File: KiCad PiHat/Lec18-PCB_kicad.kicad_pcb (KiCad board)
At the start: 2 copper layers, 65 x 56 mm, 6 parts, among them P1 Conn_02x20_Odd_Even

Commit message: Ongoing work
Continued work on schematic and PCB
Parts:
- added J4: Motor_Driver_Left, Connector_PinSocket_2.54mm:PinSocket_1x04_P2.54mm_Vertical, F.Cu at (103.5, 45.9)
- added R1: 1k, Resistor_THT:R_Axial_DIN0207_L6.3mm_D2.5mm_P7.62mm_Horizontal, F.Cu at (132.7, 76.3)
- added R2: 1k, Resistor_THT:R_Axial_DIN0207_L6.3mm_D2.5mm_P7.62mm_Horizontal, F.Cu at (125.1, 81.4)
- added R3: 1k, Resistor_THT:R_Axial_DIN0207_L6.3mm_D2.5mm_P7.62mm_Horizontal, F.Cu at (121.1, 75.1)
- A1: value Arduino_Nano_v2.x -> Arduino_Nano
- moved A1 34.1 mm to (132.7, 71.3), turned to -90 degrees
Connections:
- net +3V3 renamed Net-(P1-Pad1)
- A1 pad 1: /GPIO15(RXD0) -> /GPIO14(TXD0_5V)
- A1 pad 29: unconnected-(A1-Pad29) -> GND
- A1 pad 30: unconnected-(A1-Pad30) -> +5V
- A1 pad 4: unconnected-(A1-Pad4) -> GND
- P1 pad 10: /GPIO15(RXD0) -> /GPIO15(RXD0_3.3V)
- P1 pad 2: +5V -> Net-(P1-Pad2)
- P1 pad 4: +5V -> Net-(P1-Pad2)

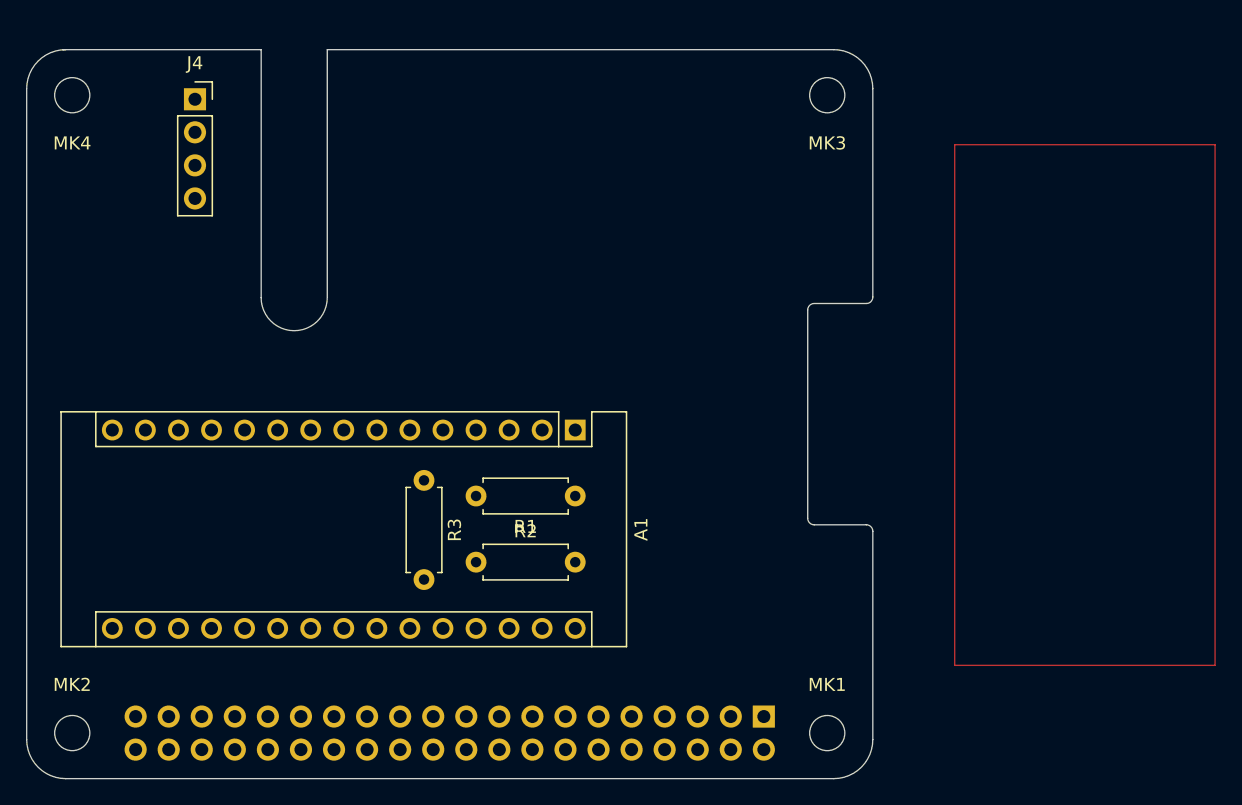
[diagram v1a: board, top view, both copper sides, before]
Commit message: Finished Schematic
Schematic finished. Sanity check and routing coming next
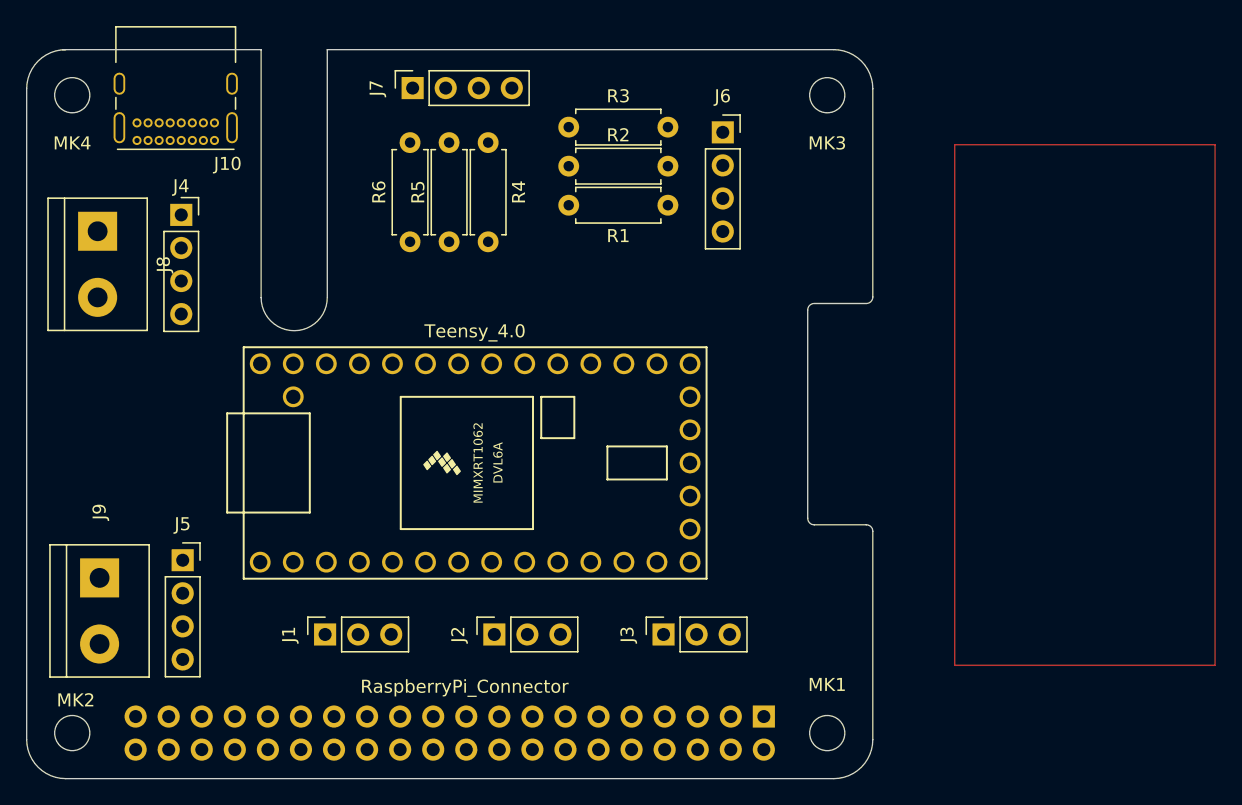
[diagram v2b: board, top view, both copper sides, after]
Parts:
- added J1: Servo_BEEG, Connector_PinSocket_2.54mm:PinSocket_1x03_P2.54mm_Vertical, F.Cu at (113.5, 87.0)
- added J10: USB_C_Receptacle_USB2.0, Connector_USB:USB_C_Receptacle_GCT_USB4085, F.Cu at (105.0, 49.0)
- added J2: Servo_SHOOT, Connector_PinSocket_2.54mm:PinSocket_1x03_P2.54mm_Vertical, F.Cu at (126.5, 87.0)
- added J3: Servo_EXTRA, Connector_PinSocket_2.54mm:PinSocket_1x03_P2.54mm_Vertical, F.Cu at (139.5, 87.0)
- added J5: Motor_Driver_Right, Connector_PinSocket_2.54mm:PinSocket_1x04_P2.54mm_Vertical, F.Cu at (102.5, 81.3)
- added J6: Ultrasonic_Front, Connector_PinSocket_2.54mm:PinSocket_1x04_P2.54mm_Vertical, F.Cu at (144.0, 48.4)
- added J7: Ultrasonic_Left, Connector_PinSocket_2.54mm:PinSocket_1x04_P2.54mm_Vertical, F.Cu at (120.2, 45.0)
- added J8: Motor_Power_Left, TerminalBlock:TerminalBlock_bornier-2_P5.08mm, F.Cu at (96.0, 56.0)
- added J9: Motor_Power_Right, TerminalBlock:TerminalBlock_bornier-2_P5.08mm, F.Cu at (96.2, 82.6)
- added R4: 1k, Resistor_THT:R_Axial_DIN0207_L6.3mm_D2.5mm_P7.62mm_Horizontal, F.Cu at (126.0, 49.2)
- added R5: 1k, Resistor_THT:R_Axial_DIN0207_L6.3mm_D2.5mm_P7.62mm_Horizontal, F.Cu at (123.0, 56.8)
- added R6: 1k, Resistor_THT:R_Axial_DIN0207_L6.3mm_D2.5mm_P7.62mm_Horizontal, F.Cu at (120.0, 56.8)
- A1: value Arduino_Nano -> Teensy_4.0; footprint Module:Arduino_Nano -> teensy:Teensy40
- P1: value Conn_02x20_Odd_Even -> RaspberryPi_Connector
- moved R2 31.2 mm to (132.2, 51.0)
- moved R3 29.3 mm to (132.2, 48.0), turned to 0 degrees
- moved R1 23.4 mm to (139.8, 54.0)
- moved J4 8.95 mm to (102.4, 54.7)
- moved A1 8.10 mm to (125.0, 73.8), turned to 0 degrees
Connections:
- net /GPIO14(TXD0) renamed /PI_to_Teensy
- A1 pad 1: /GPIO14(TXD0_5V) -> GND
- A1 pad 10: unconnected-(A1-Pad10) -> /IN2(MOTOR_LEFT)
- A1 pad 11: unconnected-(A1-Pad11) -> /IN1(MOTOR_LEFT)
- A1 pad 17: unconnected-(A1-Pad17) -> GND
- A1 pad 25: unconnected-(A1-Pad25) -> /Ultrasonic_Front_Trig
- A1 pad 26: unconnected-(A1-Pad26) -> /Ultrasonic_Front_Echo
- A1 pad 29: GND -> /Ultrasonic_Left_Trig
- A1 pad 3: unconnected-(A1-Pad3) -> /Teensy_to_PI
- A1 pad 30: +5V -> /Ultrasonic_Left_Echo
- A1 pad 4: GND -> /IN1(MOTOR_RIGHT)
- A1 pad 5: unconnected-(A1-Pad5) -> /IN2(MOTOR_RIGHT)
- A1 pad 6: unconnected-(A1-Pad6) -> /IN3(MOTOR_RIGHT)
- A1 pad 7: unconnected-(A1-Pad7) -> /IN4(MOTOR_RIGHT)
- A1 pad 8: unconnected-(A1-Pad8) -> /IN4(MOTOR_LEFT)
- A1 pad 9: unconnected-(A1-Pad9) -> /IN3(MOTOR_LEFT)
- P1 pad 10: /GPIO15(RXD0_3.3V) -> /Teensy_to_PI
- R1 pad 1: /GPIO14(TXD0_5V) -> Net-(R1-Pad1)
- R1 pad 2: /GPIO15(RXD0_3.3V) -> /Ultrasonic_Front_Echo
- R2 pad 1: Net-(R3-Pad2) -> /Ultrasonic_Front_Echo
- R2 pad 2: GND -> Net-(R2-Pad2)
- R3 pad 1: /GPIO15(RXD0_3.3V) -> Net-(R2-Pad2)
- R3 pad 2: Net-(R3-Pad2) -> GND

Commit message: routing complete
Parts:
- moved J1 1.41 mm to (112.5, 88.0)
- moved J2 1.41 mm to (125.5, 88.0)
- moved J3 1.41 mm to (138.5, 88.0)
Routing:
- net GND: track 0.00 -> 313.1 mm
- net +5V: track 0.00 -> 187.4 mm
- net /PI_to_Teensy: track 0.00 -> 50.8 mm
- net /IN1(MOTOR_LEFT): track 0.00 -> 49.0 mm
- net /IN2(MOTOR_LEFT): track 0.00 -> 44.9 mm
- net /Teensy_to_PI: track 0.00 -> 44.3 mm
- net /IN3(MOTOR_LEFT): track 0.00 -> 41.0 mm
- net /IN4(MOTOR_LEFT): track 0.00 -> 37.0 mm
- net /Ultrasonic_Left_Trig: track 0.00 -> 25.6 mm
- net /IN4(MOTOR_RIGHT): track 0.00 -> 25.4 mm
- net /Ultrasonic_Front_Trig: track 0.00 -> 21.6 mm
- net /IN3(MOTOR_RIGHT): track 0.00 -> 21.5 mm
- net /IN2(MOTOR_RIGHT): track 0.00 -> 17.7 mm
- net /Ultrasonic_Front_Echo: track 0.00 -> 17.6 mm
- net /IN1(MOTOR_RIGHT): track 0.00 -> 15.8 mm
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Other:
- board text added: "+5V"
- board text added: "GND"
- board text added: "IN1"
- board text added: "IN2"
- board text added: "IN3"
- board text added: "IN4"
- board text added: "SIG"
- board text removed: "RJ45"
- board text removed: "USB"

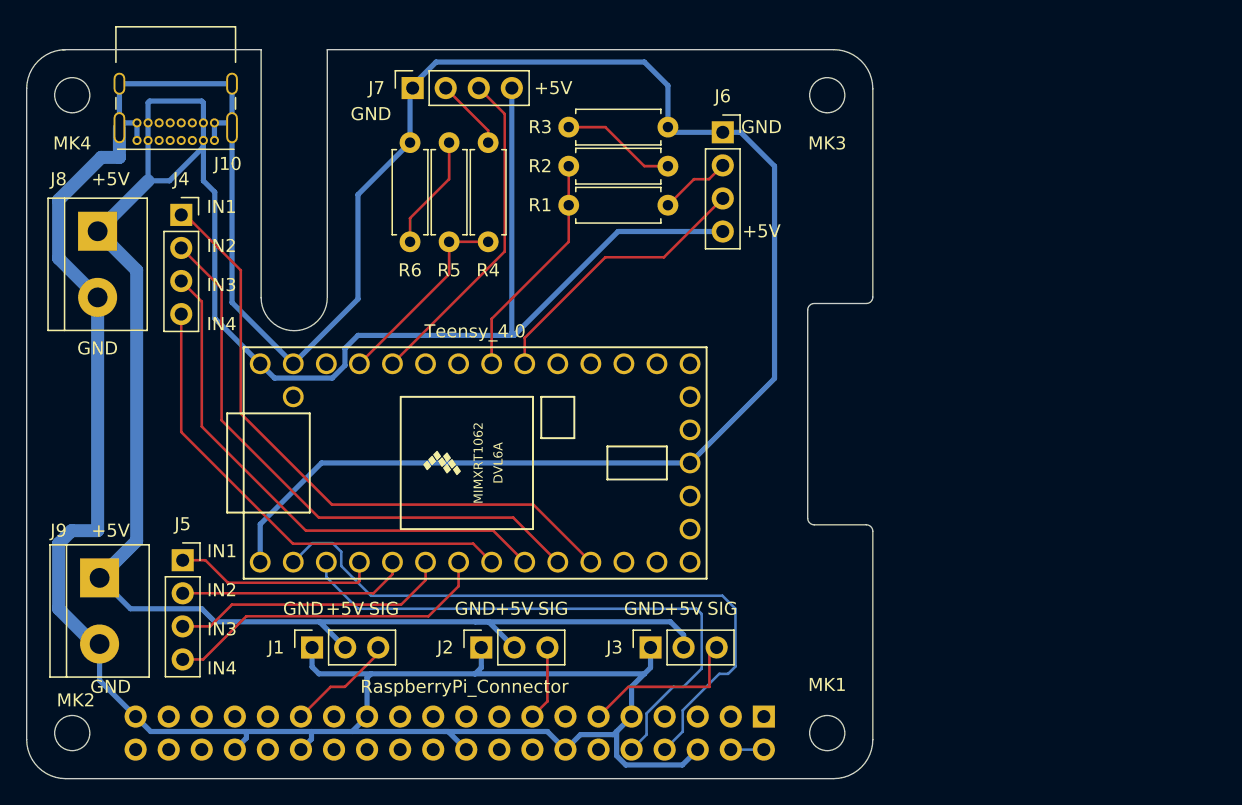
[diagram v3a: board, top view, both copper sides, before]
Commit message: PCB complete with logos and graphics
PCB work complete. Going to speak with instructor to make sure all parameters are correct before sending out to have the pcb made.
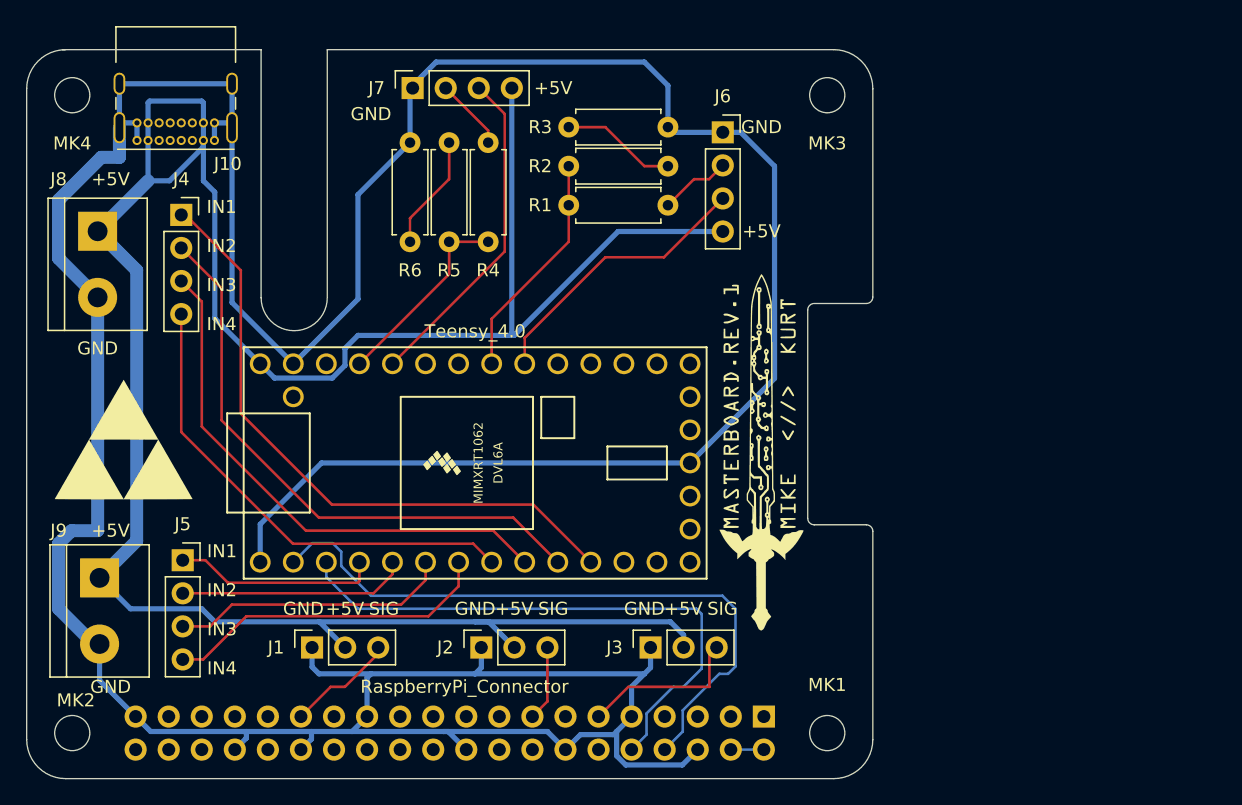
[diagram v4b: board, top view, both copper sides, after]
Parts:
- added Logo: LOGO, Other:Masterboard_Logo, F.Cu at (147.0, 73.0)
- added Triforce: LOGO, Other:Triforce, F.Cu at (98.0, 72.0)
- added image: LOGO, Other:Dangerous, B.Cu at (124.0, 74.0)
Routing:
- net unconnected-(A1-Pad22): track 0.00 -> 0.50 mm
